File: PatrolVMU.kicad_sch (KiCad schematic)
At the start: 64 parts, among them J1 C-OBD-II-16M, J2 Conn_01x03_Pin, Q1 BC549, Q2 BC549, U1 MAX232, U2 CD4060BNSR, U3 L7805, U4 LM358ST, Y1 2.4576M

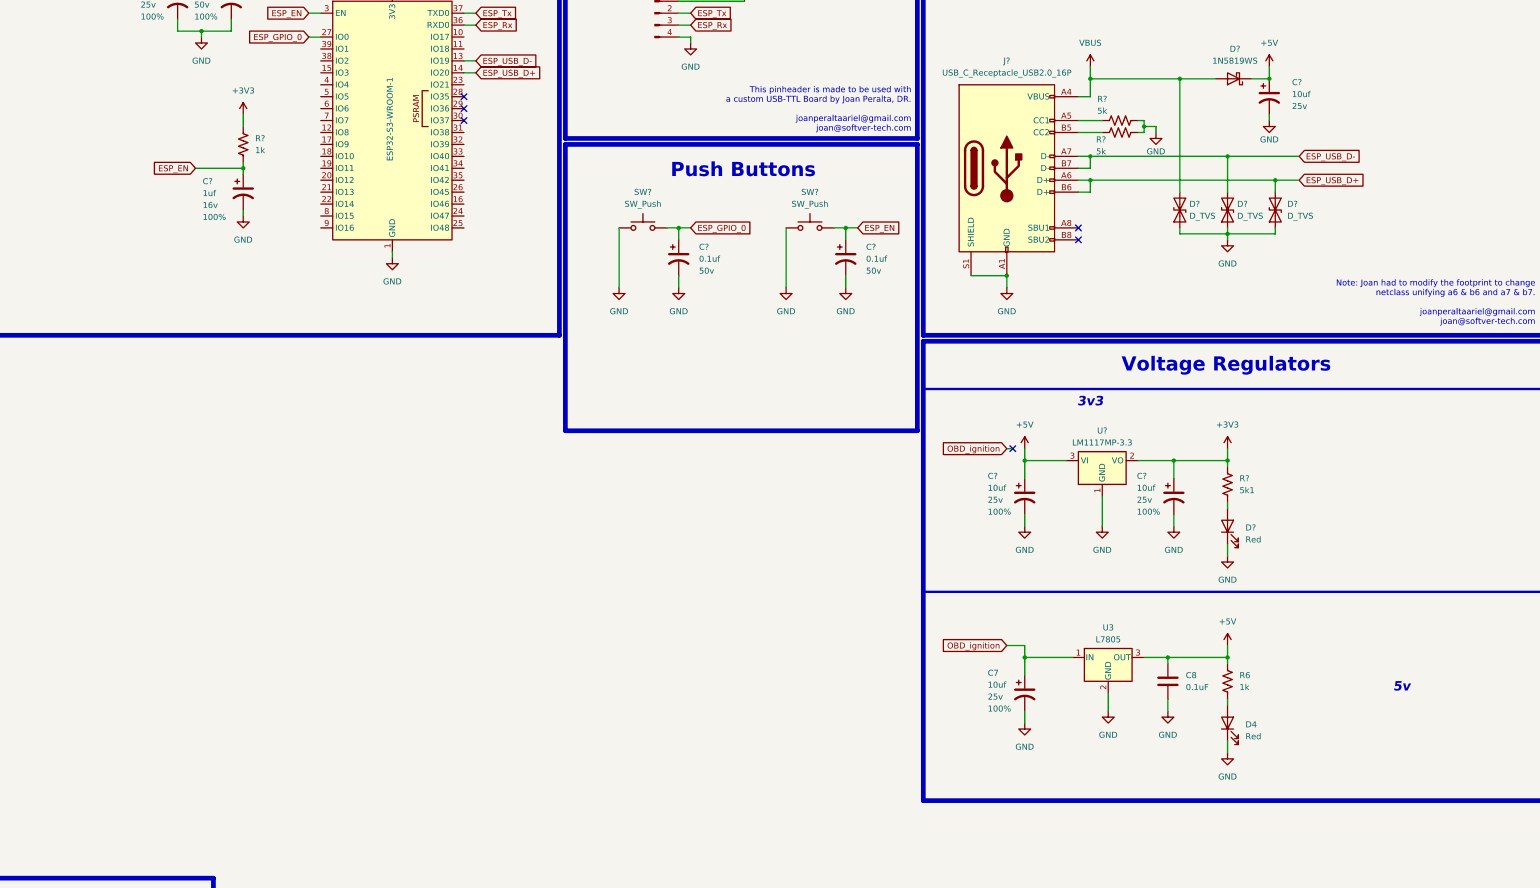
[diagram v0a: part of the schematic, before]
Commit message: added Lead Acid Monitor IC
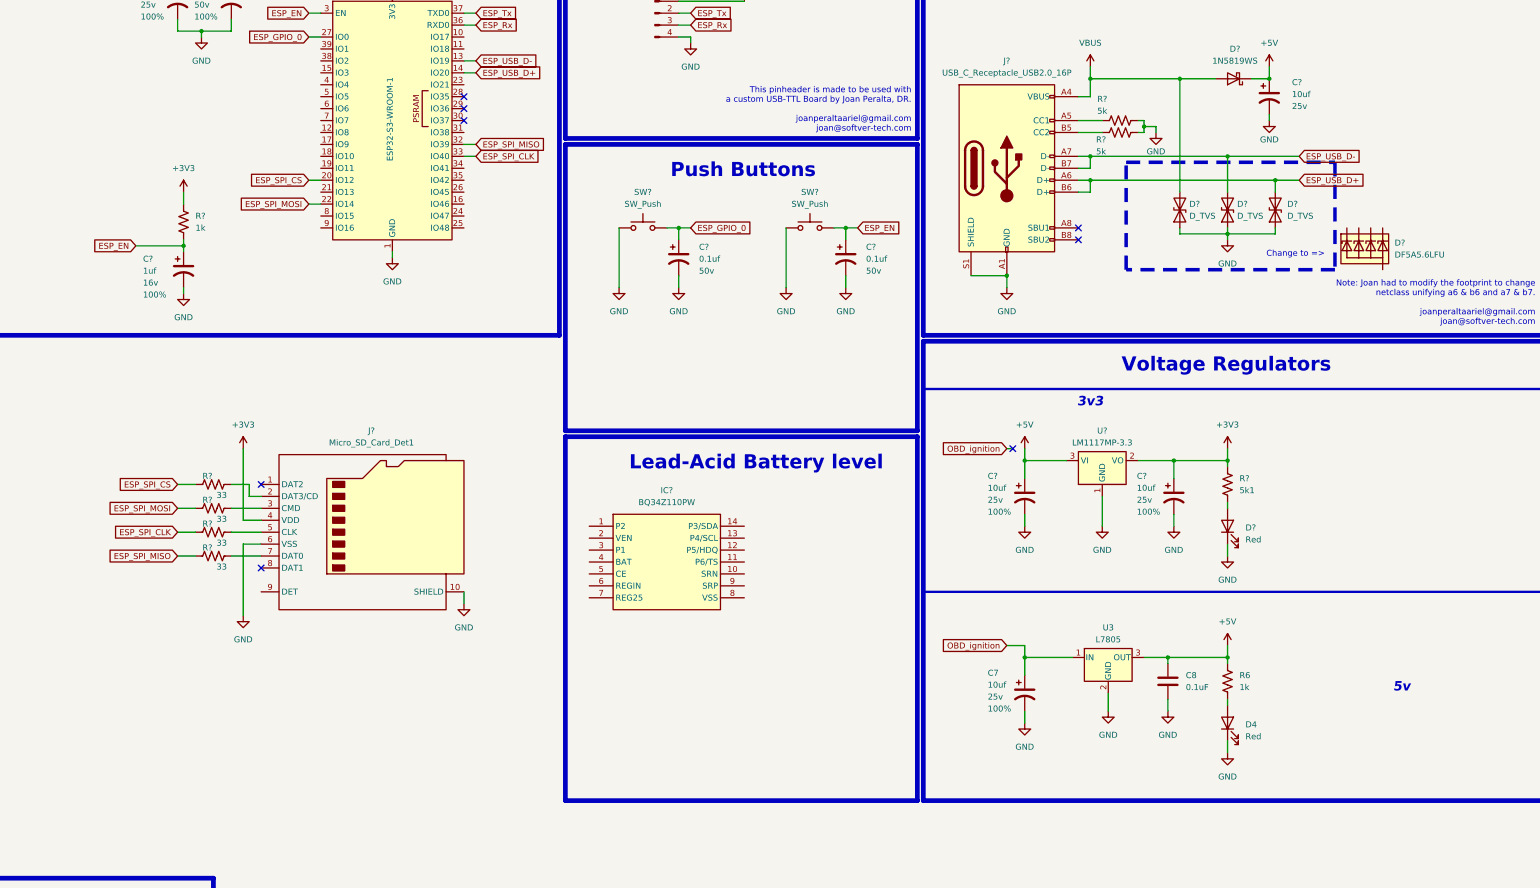
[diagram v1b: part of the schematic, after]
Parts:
- added D?: DF5A5.6LFU, SparkFun-Semiconductor-Standard:SOT-353, symbol SparkFun-DiscreteSemi:D_TVS_ESD_4_HS
- added IC?: BQ34Z110PW, SOP65P640X120-14N, symbol BQ34Z110PW:BQ34Z110PW
- added J?: Micro_SD_Card_Det1, symbol Connector:Micro_SD_Card_Det1
- added R? (x4): 33, SparkFun-Resistor:R_0402_1005Metric, symbol SparkFun-Resistor:0_0402
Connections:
- net +3V3: now also J?.4 (VDD)
- net GND: now also J?.10 (SHIELD), J?.6 (VSS)
- net ESP_SPI_CS: now reaches U?.20 (IO12)
- net ESP_SPI_CS: now also R?.1
- net ESP_SPI_MOSI: now reaches U?.22 (IO14)
- net ESP_SPI_MOSI: now also R?.1
- net ESP_SPI_MISO: now reaches U?.32 (IO39)
- net ESP_SPI_MISO: now also R?.1
- net ESP_SPI_CLK: now reaches U?.33 (IO40)
- net ESP_SPI_CLK: now also R?.1
- new net: J?.3 (CMD), R?.2
- new net: J?.5 (CLK), R?.2
- new net: J?.7 (DAT0), R?.2
- new net: J?.2 (DAT3/CD), R?.2
- no-connect marks 6 -> 8
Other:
- note added: "Change to =>"
- note added: "Lead-Acid Battery level"
- moved on the sheet: C?, R?

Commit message: making provisional connector
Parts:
- removed C1, C?: 1uf, symbol SparkFun-Capacitor:C_Polarized
- removed C2, C3, C4, C5: 1uF, symbol Device:C
- removed C? (x3): 0.1uf, symbol SparkFun-Capacitor:C_Polarized
- removed C? (x4): 10uf, symbol SparkFun-Capacitor:C_Polarized
- removed D2: Green, SparkFun-LED:LED_0603_1608Metric, symbol SparkFun-LED:LED_Red_0603
- removed D3: Yellow, SparkFun-LED:LED_0603_1608Metric, symbol SparkFun-LED:LED_Red_0603
- removed D?: DF5A5.6LFU, SparkFun-Semiconductor-Standard:SOT-353, symbol SparkFun-DiscreteSemi:D_TVS_ESD_4_HS
- removed D? (x3): D_TVS, symbol Device:D_TVS
- removed D?: Red, SparkFun-LED:LED_0603_1608Metric, symbol SparkFun-LED:LED_Red_0603
- removed D?: 1N5819WS, Diode_SMD:D_SOD-323, symbol Diode:1N5819WS
- removed IC?: BQ34Z110PW, SOP65P640X120-14N, symbol BQ34Z110PW:BQ34Z110PW
- removed J2: Conn_01x03_Pin, symbol Connector:Conn_01x03_Pin
- removed J?: USB_C_Receptacle_USB2.0_16P, symbol Connector:USB_C_Receptacle_USB2.0_16P
- removed J?: Micro_SD_Card_Det1, symbol Connector:Micro_SD_Card_Det1
- removed J?: Conn_01x04_Pin, symbol Connector:Conn_01x04_Pin
- removed JP?: ~, SparkFun-Jumper:Jumper-3_1-NC_Trace, symbol SparkFun-Jumper:SolderJumper_3_Bridged12
- removed R7, R9, R?: 1k, SparkFun-Resistor:R_0402_1005Metric, symbol SparkFun-Resistor:0_0402
- removed R? (x4): 33, SparkFun-Resistor:R_0402_1005Metric, symbol SparkFun-Resistor:0_0402
- removed R?: 5k1, SparkFun-Resistor:R_0402_1005Metric, symbol SparkFun-Resistor:0_0402
- removed R? (x2): 5k, SparkFun-Resistor:R_0402_1005Metric, symbol SparkFun-Resistor:0_0402
- removed R?: 0(1%), SparkFun-Resistor:R_0402_1005Metric, symbol SparkFun-Resistor:0_0402
- removed SW? (x2): SW_Push, symbol Switch:SW_Push
- removed U1: MAX232, symbol Interface_UART:MAX232
- removed U?: ESP32-S3-WROOM-1, RF_Module:ESP32-S3-WROOM-1, symbol RF_Module:ESP32-S3-WROOM-1
- removed U?: LM1117MP-3.3, Package_TO_SOT_SMD:SOT-223-3_TabPin2, symbol Regulator_Linear:LM1117MP-3.3
- added U?: ~, Waveshare-ESP32:Waveshare-ESP32-C3-Zero, symbol Waveshare-ESP32:Waveshare-ESP32-C3-Zero
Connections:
- net INPUT is gone; now on net ESP_Tx: R4.2
- net OUTPUT is gone; now on net ESP_Rx: R2.1
- net +5V: now also U?.1 (VCC)
- net ESP_Rx: now also U?.17 (IO20)
- net ESP_Tx: now also U?.18 (IO21)
- net ESP_USB_D+: now also U?.16 (IO19)
- net ESP_USB_D-: now also U?.15 (IO18)
- net GND: now also U?.2 (GND)
- no-connect marks 8 -> 1
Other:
- note added: "NOTE: Moving on, move to ESP32-C3-WROOM-02-N4 H4 Difference is just high temperature."
- note added: "Poka-Yoke"
- note added: "Voltage Regulator"
- note added: "Waveshare ESP32-C3 Zero"
- note removed: "3v3"
- note removed: "Change to =>"
- note removed: "ESP32-WROOM-1"
- note removed: "Lead-Acid Battery level"
- note removed: "Note: Joan had to modify the footprint to change netclass unifying a6 & b6 and a7 & b7. joanperaltaariel@gmail.com joan@softver-tech.com"
- note removed: "Push Buttons"
- note removed: "This pinheader is made to be used with a custom USB-TTL Board by Joan Peralta, DR. joanperaltaariel@gmail.com joan@softver-tech.com"
- note removed: "To Serial (Consult II)"
- note removed: "USB-C"
- note removed: "USB-TTL"
- note removed: "Voltage Regulators"
- moved on the sheet: C7, C8, D4, R6, U3

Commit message: finished preliminarly
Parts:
- removed Q1, Q2: BC549, Package_TO_SOT_THT:TO-92_Inline, symbol Transistor_BJT:BC549
- added C1, C3: 100nf, Capacitor_SMD:C_0805_2012Metric, symbol Device:C
- added C2: 10nf, Capacitor_SMD:C_0805_2012Metric, symbol Device:C
- added D1, D2: SMBJ26A, Diode_SMD:D_SMB, symbol Diode:SM6T27A
- added Q1, Q2: BC549CTA, BC549CTA:BC33740TA, symbol BC549CTA:BC549CTA
- added R15, R16, R17, R19, R7, R9: 10k, Capacitor_SMD:C_0805_2012Metric, symbol Device:R
- added R18: 100, Resistor_SMD:R_2512_6332Metric, symbol Device:R
- added R20: 200k, Capacitor_SMD:C_0805_2012Metric, symbol Device:R
- added R21: 33k, Capacitor_SMD:C_0805_2012Metric, symbol Device:R
- added R22: 1M, Capacitor_SMD:C_0805_2012Metric, symbol Device:R
- added R23, R24: 180k, Capacitor_SMD:C_0805_2012Metric, symbol Device:R
- added U5: INA226, Package_SO:VSSOP-10_3x3mm_P0.5mm, symbol Sensor_Energy:INA226
- added U6: TLV7031DBV, Package_TO_SOT_SMD:SOT-23-5, symbol Comparator:TLV7031DBV
- C10, C11, C12, C13, C7, C8, C9: footprint (none) -> Capacitor_SMD:C_0805_2012Metric
- D4: footprint SparkFun-LED:LED_0603_1608Metric -> LED_SMD:LED_0805_2012Metric
- J2: renamed from J?; footprint (none) -> Jumper:SolderJumper-3_P1.3mm_Bridged2Bar12_Pad1.0x1.5mm
- R1, R10, R11, R12, R13, R14, R2, R3, R4, R5, R6, R8: footprint SparkFun-Resistor:R_0402_1005Metric -> Capacitor_SMD:C_0805_2012Metric
- U1: renamed from U?; value ~ -> ESP32-C3
- U2: footprint SOIC127P780X200-16N -> CD4060BNSR:SOIC127P780X200-16N
- U3: footprint (none) -> Package_TO_SOT_SMD:TO-263-2
- U4: footprint SOP65P490X110-8N -> LM358ST:SOP65P490X110-8N
- Y1: footprint SparkFun-Clock:Crystal-SMD-5x3.2mm -> Crystal:Crystal_HC49-4H_Vertical
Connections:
- net +5V: now also C11.1, U2.16 (VDD), C1.1, U5.6 (VS)
- net GND: now also C1.2, C2.2, C3.2, D1.2 (A2), D2.2 (A2), Q1.3 (E), Q2.3 (E), R17.1, R21.2, R24.2, R7.1, U5.7 (GND), U6.2 (V-)
- net OBD_clock: now also Q2.1 (C)
- net OBD_ignition: now also R19.2; no longer C7.1, U3.1 (IN)
- net OBD_rx: now also Q1.1 (C)
- net at J2.1 (Pin_1): now also U2.5 (Q5); no longer U2.7 (Q4)
- net at J2.3 (Pin_3): now also U2.7 (Q4); no longer U2.5 (Q5)
- net at R4.1, R5.1: now also Q1.2 (B)
- net at C10.1, R8.1, U2.10 (~{O}): now also Y1.1; no longer Y1.2
- net at R11.2, R12.1: now also Q2.2 (B)
- net at C9.1, R8.2, U2.11 (I): now also Y1.2; no longer Y1.1
- net OBD_12v: now reaches J1.16
- net OBD_12v: now also C7.1, U3.1 (IN), D1.1 (A1), R18.1, U5.8 (Vbus), U5.9 (Vin-)
- net ESP_I2C_SDA: now reaches U1.12 (IO8)
- net ESP_I2C_SDA: now also R15.2, U5.4 (SDA)
- net ESP_I2C_SCL: now reaches U1.13 (IO9)
- net ESP_I2C_SCL: now also R16.2, U5.5 (SCL)
- net +3.3V: now reaches U1.3 (V3V)
- net +3.3V: now also R15.1, R16.1, R22.1, R23.1, R9.1, U6.5 (V+)
- net OBD_IGN_SIG: now reaches U1.4 (IO0)
- net OBD_IGN_SIG: now also R22.2, U6.1
- new net: R9.2, U5.3 (~{Alert})
- new net: C2.1, D2.1 (A1), R19.1, R20.2
- new net: C3.1, R23.2, R24.1, U6.4 (-)
- new net: R20.1, R21.1, U6.3 (+)
- new net: R17.2, U5.2 (A0)
- new net: R7.2, U5.1 (A1)
- new net: R18.2, U5.10 (Vin+)
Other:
- note added: "Battery Voltge Level"
- note added: "Ignition Detection"
- moved on the sheet: C10, C11, C12, C13, C7, C8, C9, D4, J1, J2, R1, R10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

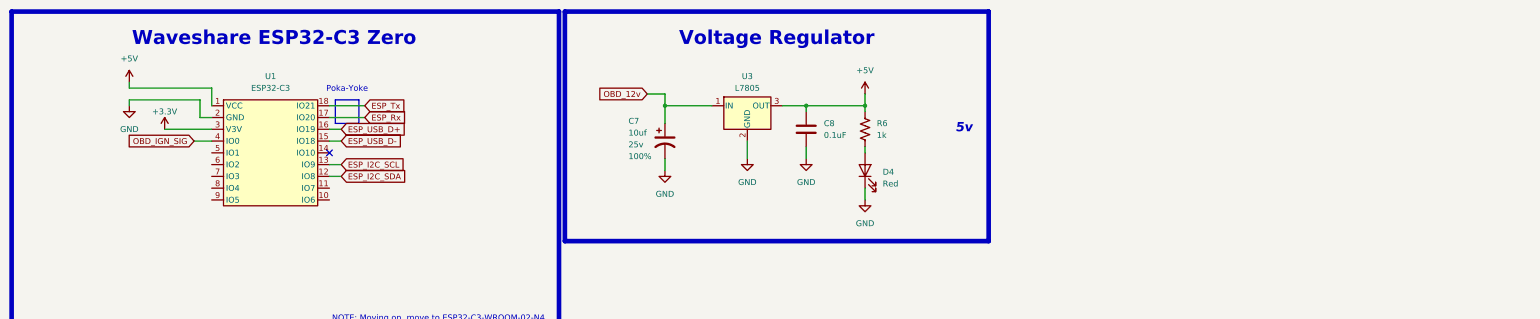
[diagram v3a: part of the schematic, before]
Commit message: fixed texts, added mt holes, etc
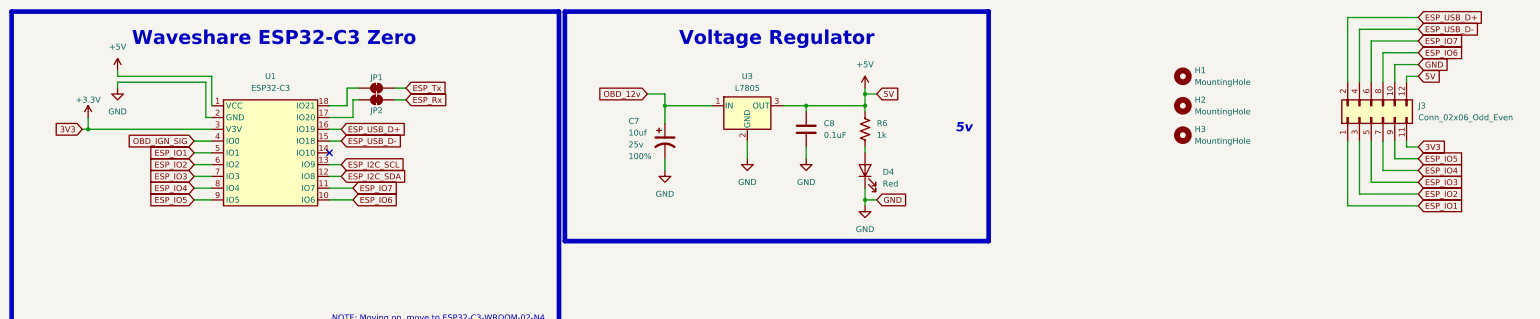
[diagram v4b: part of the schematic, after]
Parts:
- added H1, H2, H3: MountingHole, MountingHole:MountingHole_2.2mm_M2, symbol Mechanical:MountingHole
- added J3: Conn_02x06_Odd_Even, Connector_PinHeader_2.54mm:PinHeader_2x06_P2.54mm_Vertical, symbol Connector_Generic:Conn_02x06_Odd_Even
- added JP1, JP2: SolderJumper_2_Bridged, Jumper:SolderJumper-2_P1.3mm_Bridged2Bar_Pad1.0x1.5mm, symbol Jumper:SolderJumper_2_Bridged
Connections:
- net +3.3V: now also J3.11 (Pin_11)
- net +5V: now also J3.12 (Pin_12)
- net ESP_Rx: now also JP2.2 (B); no longer U1.17 (IO20)
- net ESP_Tx: now also JP1.2 (B); no longer U1.18 (IO21)
- net ESP_USB_D+: now also J3.2 (Pin_2)
- net ESP_USB_D-: now also J3.4 (Pin_4)
- net GND: now also J3.10 (Pin_10)
- net ESP_IO6: now reaches U1.10 (IO6)
- net ESP_IO6: now also J3.8 (Pin_8)
- net ESP_IO7: now reaches U1.11 (IO7)
- net ESP_IO7: now also J3.6 (Pin_6)
- net ESP_IO1: now reaches U1.5 (IO1)
- net ESP_IO1: now also J3.1 (Pin_1)
- net ESP_IO2: now reaches U1.6 (IO2)
- net ESP_IO2: now also J3.3 (Pin_3)
- net ESP_IO3: now reaches U1.7 (IO3)
- net ESP_IO3: now also J3.5 (Pin_5)
- net ESP_IO4: now reaches U1.8 (IO4)
- net ESP_IO4: now also J3.7 (Pin_7)
- net ESP_IO5: now reaches U1.9 (IO5)
- net ESP_IO5: now also J3.9 (Pin_9)
- new net: JP1.1 (A), U1.18 (IO21)
- new net: JP2.1 (A), U1.17 (IO20)
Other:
- note removed: "Poka-Yoke"
